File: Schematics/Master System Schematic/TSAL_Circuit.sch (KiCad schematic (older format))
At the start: 0 parts

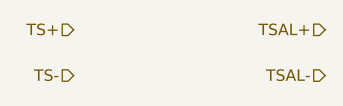
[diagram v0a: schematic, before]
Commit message: Updated TSAL
Updated TSAL to now also tap from inside the AIRs
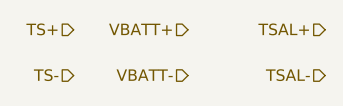
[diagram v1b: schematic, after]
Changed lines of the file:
@@
 $Descr A4 11693 8268
 encoding utf-8
-Sheet 9 13
+Sheet 13 13
 Title ""
 Date "2020-10-12"
@@
 Text HLabel 3650 3650 0    50   Input ~ 0
 TSAL-
+Text HLabel 3050 3450 0    50   Input ~ 0
+VBATT+
+Text HLabel 3050 3650 0    50   Input ~ 0
+VBATT-
 $EndSCHEMATC
